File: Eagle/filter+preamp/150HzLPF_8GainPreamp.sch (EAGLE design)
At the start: 25 parts, among them U1 LM358, U2 LM358

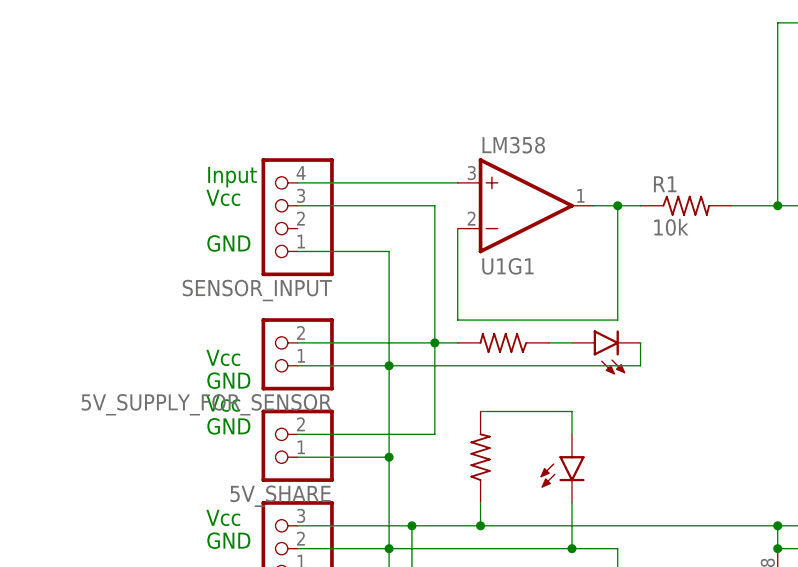
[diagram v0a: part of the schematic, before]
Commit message: add passcon
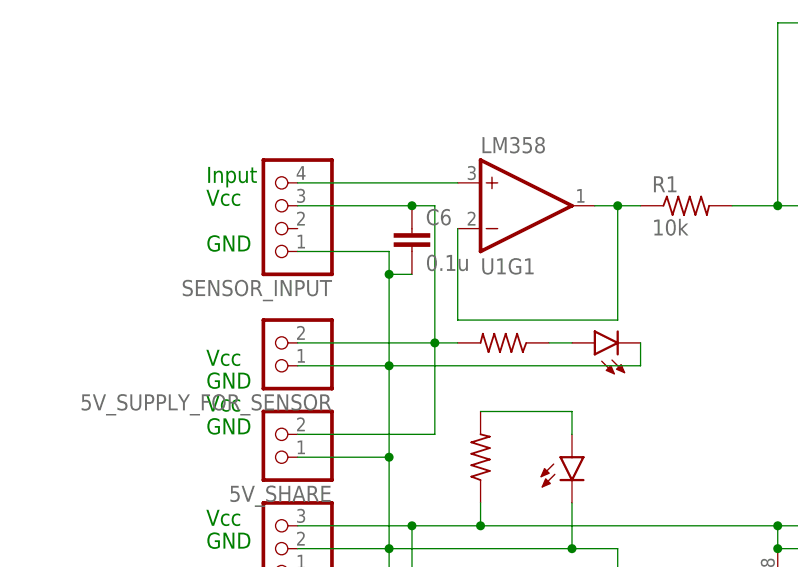
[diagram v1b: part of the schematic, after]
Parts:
- added C6: 0.1u, rcl:C-EUC0603
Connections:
- net N$6 renamed 18V_VCC
- removed net N$15: 5V_SHARE.2, 5V_SUPPLY_FOR_SENSOR.2, R8.2, SENSOR_INPUT.3
- removed net N$17: 18V_SHARE.2, 18V_SUPPLY_FOR_OPEAMP.2, 5V_SHARE.1, 5V_SUPPLY_FOR_SENSOR.1, C1.2, C5.-, C8.2, C9.2, D2.C, D3.C, R6.1, SENSOR_INPUT.1, SENSOR_OUTPUT.2, U1G3.P$V-, U2G3.P$V-
- new net 5V_VCC: 5V_SHARE.2, 5V_SUPPLY_FOR_SENSOR.2, C6.1, R8.2, SENSOR_INPUT.3
- new net GND: 18V_SHARE.2, 18V_SUPPLY_FOR_OPEAMP.2, 5V_SHARE.1, 5V_SUPPLY_FOR_SENSOR.1, C1.2, C5.-, C6.2, C8.2, C9.2, D2.C, D3.C, R6.1, SENSOR_INPUT.1, SENSOR_OUTPUT.2, U1G3.P$V-, U2G3.P$V-
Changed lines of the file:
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@@
 <part name="D3" library="LED" library_urn="urn:adsk.eagle:library:11396303" deviceset="LTL-1CHE" device="" package3d_urn="urn:adsk.eagle:package:10893502/2"/>
 <part name="R9" library="rcl" library_urn="urn:adsk.eagle:library:334" deviceset="R-US_" device="0207/7" package3d_urn="urn:adsk.eagle:package:23493/2" value="3.3k"/>
+<part name="C6" library="rcl" library_urn="urn:adsk.eagle:library:334" deviceset="C-EU" device="C0603" package3d_urn="urn:adsk.eagle:package:23616/2" value="0.1u"/>
 </parts>
 <sheets>
@@
 <instance part="D3" gate="G$1" x="22.86" y="40.64" smashed="yes"/>
 <instance part="R9" gate="G$1" x="12.7" y="40.64" smashed="yes" rot="R90"/>
+<instance part="C6" gate="G$1" x="5.08" y="66.04" smashed="yes">
+<attribute name="NAME" x="6.604" y="66.421" size="1.778" layer="95"/>
+<attribute name="VALUE" x="6.604" y="61.341" size="1.778" layer="96"/>
+</instance>
 </instances>
 <busses>
@@
 </segment>
 </net>
-<net name="N$6" class="0">
+<net name="18V_VCC" class="0">
 <segment>
 <pinref part="R5" gate="G$1" pin="1"/>
@@
 </segment>
 </net>
-<net name="N$17" class="0">
+<net name="GND" class="0">
 <segment>
 <pinref part="C5" gate="G$1" pin="-"/>
@@
 <wire x1="66.04" y1="45.72" x2="66.04" y2="12.7" width="0.1524" layer="91"/>
 <wire x1="27.94" y1="30.48" x2="27.94" y2="12.7" width="0.1524" layer="91"/>
-<wire x1="2.54" y1="63.5" x2="2.54" y2="50.8" width="0.1524" layer="91"/>
+<wire x1="2.54" y1="63.5" x2="2.54" y2="60.96" width="0.1524" layer="91"/>
+<wire x1="2.54" y1="60.96" x2="2.54" y2="50.8" width="0.1524" layer="91"/>
 <wire x1="2.54" y1="50.8" x2="2.54" y2="40.64" width="0.1524" layer="91"/>
 <wire x1="2.54" y1="40.64" x2="2.54" y2="30.48" width="0.1524" layer="91"/>
@@
 <wire x1="22.86" y1="35.56" x2="22.86" y2="30.48" width="0.1524" layer="91"/>
 <junction x="22.86" y="30.48"/>
-</segment>
-</net>
-<net name="N$15" class="0">
-<segment>
-<wire x1="-7.62" y1="68.58" x2="7.62" y2="68.58" width="0.1524" layer="91"/>
+<pinref part="C6" gate="G$1" pin="2"/>
+<wire x1="5.08" y1="60.96" x2="2.54" y2="60.96" width="0.1524" layer="91"/>
+<junction x="2.54" y="60.96"/>
+</segment>
+</net>
+<net name="5V_VCC" class="0">
+<segment>
+<wire x1="-7.62" y1="68.58" x2="5.08" y2="68.58" width="0.1524" layer="91"/>
+<wire x1="5.08" y1="68.58" x2="7.62" y2="68.58" width="0.1524" layer="91"/>
 <wire x1="7.62" y1="68.58" x2="7.62" y2="53.34" width="0.1524" layer="91"/>
 <pinref part="5V_SUPPLY_FOR_SENSOR" gate="G$1" pin="2"/>
@@
 <pinref part="R8" gate="G$1" pin="2"/>
 <wire x1="7.62" y1="53.34" x2="10.16" y2="53.34" width="0.1524" layer="91"/>
-</segment>
-</net>
+<pinref part="C6" gate="G$1" pin="1"/>
+<junction x="5.08" y="68.58"/>
+</segment>
+</net>
